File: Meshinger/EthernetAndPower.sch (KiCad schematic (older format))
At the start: 12 parts, among them IC1 FAN53610AUC33X, J1 USB_A, J4 Barrel_Jack_Switch, J5 RJ45_Amphenol_RJMG1BD3B8K1ANR, J6 Conn_02x01, J7 Conn_01x04, U6 1043, U7 1043

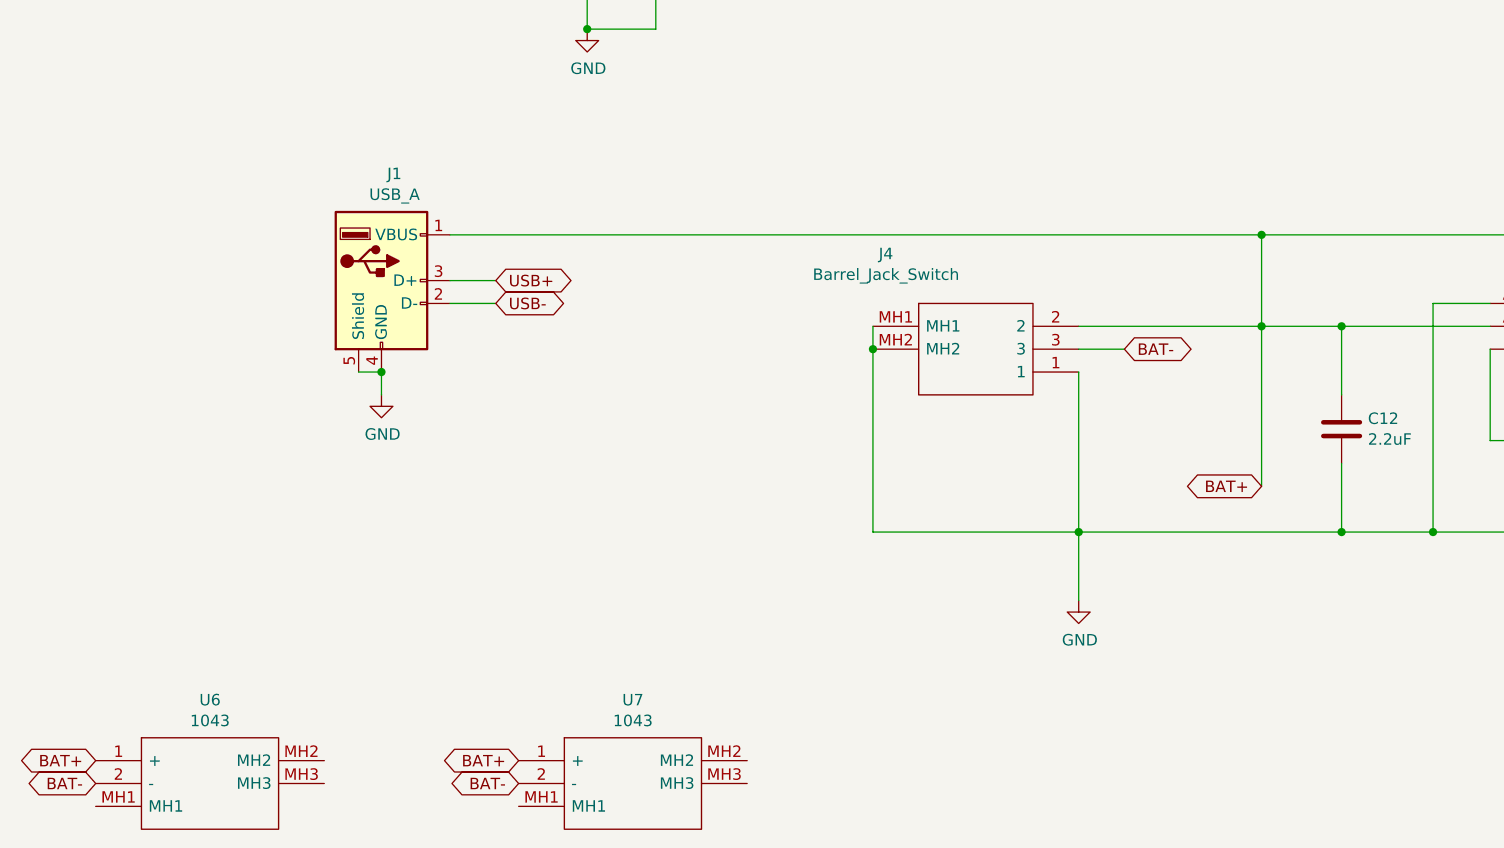
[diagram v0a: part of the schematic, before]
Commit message: Meshinger 1.0 rev C, Display Power MOSFET heats up while off...
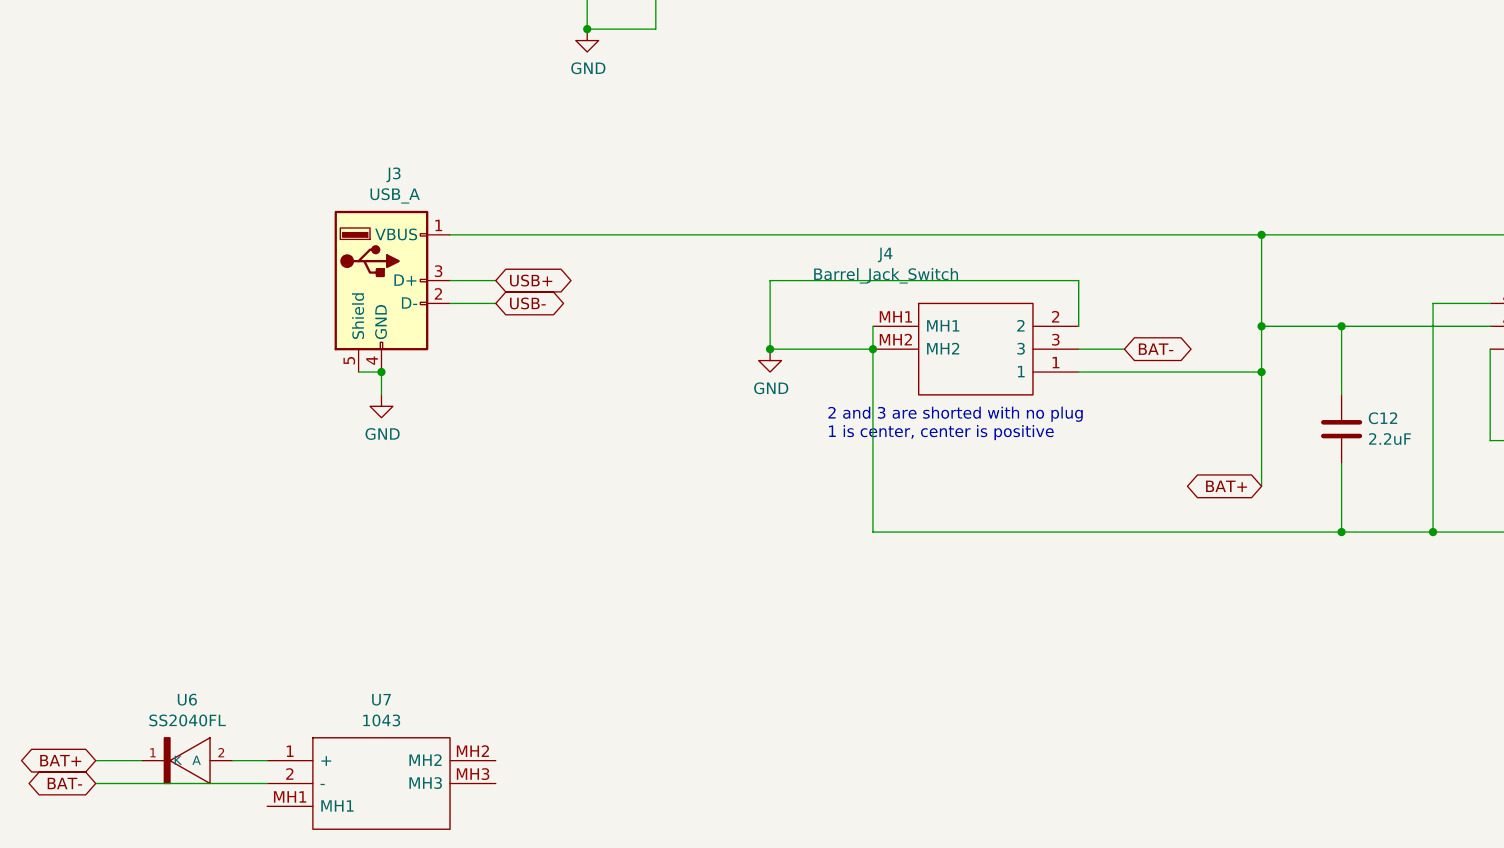
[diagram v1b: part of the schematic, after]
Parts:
- removed U7: 1043, 1043, symbol SamacSys_Parts:1043
- added U6: SS2040FL, SOD-123FL, symbol SS2040FL:SS2040FL
- renumbered J1 to J3, U6 to U7
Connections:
- net BAT+: now also J4.1, U6.1 (K); no longer J4.2, U7.1 (+)
- net GND: now also J4.2; no longer J4.1
- new net: U6.2 (A), U7.1 (+)
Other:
- note added: "2 and 3 are shorted with no plug\n1 is center, center is positive"
- moved on the sheet: U7
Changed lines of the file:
@@
 P 5500 2850
 AR Path="/6040E803/606C8F86" Ref="#PWR?"  Part="1"
-AR Path="/606A5CC1/606C8F86" Ref="#PWR0102"  Part="1"
-F 0 "#PWR0102" H 5500 2600 50  0001 C CNN
+AR Path="/606A5CC1/606C8F86" Ref="#PWR020"  Part="1"
+F 0 "#PWR020" H 5500 2600 50  0001 C CNN
 F 1 "GND" H 5505 2677 50  0000 C CNN
 F 2 "" H 5500 2850 50  0001 C CNN
@@
 P 3300 3250
 AR Path="/6040E803/606C8FA6" Ref="#PWR?"  Part="1"
-AR Path="/606A5CC1/606C8FA6" Ref="#PWR0114"  Part="1"
-F 0 "#PWR0114" H 3300 3000 50  0001 C CNN
+AR Path="/606A5CC1/606C8FA6" Ref="#PWR018"  Part="1"
+F 0 "#PWR018" H 3300 3000 50  0001 C CNN
 F 1 "GND" H 3305 3077 50  0000 C CNN
 F 2 "" H 3300 3250 50  0001 C CNN
@@
 $EndComp
 $Comp
-L Connector:USB_A J1
+L Connector:USB_A J3
 U 1 1 606D792E
 P 2400 4350
-F 0 "J1" H 2457 4817 50  0000 C CNN
+F 0 "J3" H 2457 4817 50  0000 C CNN
 F 1 "USB_A" H 2457 4726 50  0000 C CNN
 F 2 "Connector_USB:USB_A_Stewart_SS-52100-001_Horizontal" H 2550 4300 50  0001 C CNN
@@
 	2300 4750 2400 4750
 $Comp
-L power:GND #PWR0118
+L power:GND #PWR017
 U 1 1 606DDE92
 P 2400 4850
-F 0 "#PWR0118" H 2400 4600 50  0001 C CNN
+F 0 "#PWR017" H 2400 4600 50  0001 C CNN
 F 1 "GND" H 2405 4677 50  0000 C CNN
 F 2 "" H 2400 4850 50  0001 C CNN
@@
 	5450 4650 5650 4650
 $Comp
-L power:GND #PWR0119
+L power:GND #PWR019
 U 1 1 606F6FA3
-P 5450 5750
-F 0 "#PWR0119" H 5450 5500 50  0001 C CNN
-F 1 "GND" H 5455 5577 50  0000 C CNN
-F 2 "" H 5450 5750 50  0001 C CNN
-F 3 "" H 5450 5750 50  0001 C CNN
-	1    5450 5750
-	1    0    0    -1
-$EndComp
-Wire Wire Line
-	6250 5250 6250 4550
-Wire Wire Line
-	5450 4550 6250 4550
+P 4100 4650
+F 0 "#PWR019" H 4100 4400 50  0001 C CNN
+F 1 "GND" H 4105 4477 50  0000 C CNN
+F 2 "" H 4100 4650 50  0001 C CNN
+F 3 "" H 4100 4650 50  0001 C CNN
+	1    4100 4650
+	1    0    0    -1
+$EndComp
+Wire Wire Line
+	6250 5250 6250 4750
 Connection ~ 6250 4550
 Wire Wire Line
 	6250 4550 6250 4150
 Wire Wire Line
-	5450 4750 5450 5450
-Wire Wire Line
 	7250 4450 7000 4450
-Connection ~ 5450 5450
-Wire Wire Line
-	5450 5450 5450 5750
 Wire Wire Line
 	8350 4150 8350 4450
@@
 Wire Wire Line
 	7000 4450 7000 5450
-Wire Wire Line
-	5450 5450 6600 5450
 Connection ~ 7000 5450
 Wire Wire Line
@@
 Connection ~ 9550 5050
 $Comp
-L power:+3.3V #PWR0121
+L power:+3.3V #PWR022
 U 1 1 6073C0C4
 P 10350 5050
-F 0 "#PWR0121" H 10350 4900 50  0001 C CNN
+F 0 "#PWR022" H 10350 4900 50  0001 C CNN
 F 1 "+3.3V" H 10365 5223 50  0000 C CNN
 F 2 "" H 10350 5050 50  0001 C CNN
@@
 	9550 5050 10350 5050
 $Comp
-L power:GND #PWR0122
+L power:GND #PWR021
 U 1 1 607590C0
 P 7250 2050
-F 0 "#PWR0122" H 7250 1800 50  0001 C CNN
+F 0 "#PWR021" H 7250 1800 50  0001 C CNN
 F 1 "GND" H 7255 1877 50  0000 C CNN
 F 2 "" H 7250 2050 50  0001 C CNN
@@
 Wire Wire Line
 	4550 4650 4550 5450
-Wire Wire Line
-	4550 5450 5450 5450
 Connection ~ 4550 4650
 $Comp
@@
 BAT+
 $Comp
-L SamacSys_Parts:1043 U6
+L SamacSys_Parts:1043 U7
 U 1 1 60752788
-P 1150 6450
-F 0 "U6" H 1650 6715 50  0000 C CNN
-F 1 "1043" H 1650 6624 50  0000 C CNN
-F 2 "1043" H 2000 6550 50  0001 L CNN
-F 3 "http://www.keyelco.com/product-pdf.cfm?p=919" H 2000 6450 50  0001 L CNN
-F 4 "KEYSTONE - 1043 - BATTERY HOLDER, 18650, TH" H 2000 6350 50  0001 L CNN "Description"
-F 5 "14.86" H 2000 6250 50  0001 L CNN "Height"
-F 6 "534-1043" H 2000 6150 50  0001 L CNN "Mouser Part Number"
-F 7 "https://www.mouser.co.uk/ProductDetail/Keystone-Electronics/1043?qs=%2F7TOpeL5Mz6j%2FnxeOA1rsg%3D%3D" H 2000 6050 50  0001 L CNN "Mouser Price/Stock"
-F 8 "Keystone Electronics" H 2000 5950 50  0001 L CNN "Manufacturer_Name"
-F 9 "1043" H 2000 5850 50  0001 L CNN "Manufacturer_Part_Number"
-	1    1150 6450
-	1    0    0    -1
-$EndComp
-$Comp
-L SamacSys_Parts:1043 U7
-U 1 1 60753BFA
-P 3000 6450
-F 0 "U7" H 3500 6715 50  0000 C CNN
-F 1 "1043" H 3500 6624 50  0000 C CNN
-F 2 "1043" H 3850 6550 50  0001 L CNN
-F 3 "http://www.keyelco.com/product-pdf.cfm?p=919" H 3850 6450 50  0001 L CNN
-F 4 "KEYSTONE - 1043 - BATTERY HOLDER, 18650, TH" H 3850 6350 50  0001 L CNN "Description"
-F 5 "14.86" H 3850 6250 50  0001 L CNN "Height"
-F 6 "534-1043" H 3850 6150 50  0001 L CNN "Mouser Part Number"
-F 7 "https://www.mouser.co.uk/ProductDetail/Keystone-Electronics/1043?qs=%2F7TOpeL5Mz6j%2FnxeOA1rsg%3D%3D" H 3850 6050 50  0001 L CNN "Mouser Price/Stock"
-F 8 "Keystone Electronics" H 3850 5950 50  0001 L CNN "Manufacturer_Name"
-F 9 "1043" H 3850 5850 50  0001 L CNN "Manufacturer_Part_Number"
-	1    3000 6450
-	1    0    0    -1
-$EndComp
-Text GLabel 3000 6450 0    50   BiDi ~ 0
-BAT+
-Text GLabel 3000 6550 0    50   BiDi ~ 0
-BAT-
+P 1900 6450
+F 0 "U7" H 2400 6715 50  0000 C CNN
+F 1 "1043" H 2400 6624 50  0000 C CNN
+F 2 "1043" H 2750 6550 50  0001 L CNN
+F 3 "http://www.keyelco.com/product-pdf.cfm?p=919" H 2750 6450 50  0001 L CNN
+F 4 "KEYSTONE - 1043 - BATTERY HOLDER, 18650, TH" H 2750 6350 50  0001 L CNN "Description"
+F 5 "14.86" H 2750 6250 50  0001 L CNN "Height"
+F 6 "534-1043" H 2750 6150 50  0001 L CNN "Mouser Part Number"
+F 7 "https://www.mouser.co.uk/ProductDetail/Keystone-Electronics/1043?qs=%2F7TOpeL5Mz6j%2FnxeOA1rsg%3D%3D" H 2750 6050 50  0001 L CNN "Mouser Price/Stock"
+F 8 "Keystone Electronics" H 2750 5950 50  0001 L CNN "Manufacturer_Name"
+F 9 "1043" H 2750 5850 50  0001 L CNN "Manufacturer_Part_Number"
+	1    1900 6450
+	1    0    0    -1
+$EndComp
 Text GLabel 1150 6450 0    50   BiDi ~ 0
 BAT+
@@
 Text GLabel 8150 3050 2    50   BiDi ~ 0
 BAT+
+Text Notes 4350 5050 0    50   ~ 0
+2 and 3 are shorted with no plug\n1 is center, center is positive
+Wire Wire Line
+	4550 5450 6600 5450
+Wire Wire Line
+	5450 4750 6250 4750
+Connection ~ 6250 4750
+Wire Wire Line
+	6250 4750 6250 4550
+Wire Wire Line
+	4100 4650 4100 4350
+Wire Wire Line
+	4100 4350 5450 4350
+Wire Wire Line
+	5450 4350 5450 4550
+Wire Wire Line
+	4550 4650 4100 4650
+Connection ~ 4100 4650
+$Comp
+L SS2040FL:SS2040FL U?
+U 1 1 60FB3A37
+P 1550 6450
+AR Path="/6039D4D4/60FB3A37" Ref="U?"  Part="1"
+AR Path="/606A5CC1/60FB3A37" Ref="U6"  Part="1"
+F 0 "U6" H 1550 6715 50  0000 C CNN
+F 1 "SS2040FL" H 1550 6624 50  0000 C CNN
+F 2 "SOD-123FL" H 1550 6450 50  0001 L BNN
+F 3 "" H 1550 6450 50  0001 L BNN
+	1    1550 6450
+	1    0    0    -1
+$EndComp
+Wire Wire Line
+	1750 6450 1900 6450
+Wire Wire Line
+	1150 6450 1350 6450
+Wire Wire Line
+	1150 6550 1900 6550
 $EndSCHEMATC

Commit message: Meshinger 1.0 rev D, now with power switch and squiggles.
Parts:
- added S1: 1825232-1, 18252321, symbol SamacSys_Parts:1825232-1
- J7: value Conn_01x04 -> Conn_01x03; footprint Connector_PinHeader_2.54mm:PinHeader_1x04_P2.54mm_Vertical -> Connector_PinHeader_2.54mm:PinHeader_1x03_P2.54mm_Vertical; symbol Connector_Generic:Conn_01x04 -> Connector_Generic:Conn_01x03
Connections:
- net GND: now also J7.1 (Pin_1), S1.1, S1.MH1, S1.MH2; no longer J7.2 (Pin_2)
- net HW_RESET: now also S1.2; no longer J7.1 (Pin_1)
- net UART_RX: now also J7.3 (Pin_3); no longer J7.4 (Pin_4)
- net UART_TX: now also J7.2 (Pin_2); no longer J7.3 (Pin_3)
- no-connect marks 2 -> 3
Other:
- moved on the sheet: J6
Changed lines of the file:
@@
 L Connector_Generic:Conn_02x01 J?
 U 1 1 606C8F7A
-P 7850 3050
+P 6900 2700
 AR Path="/6040E803/606C8F7A" Ref="J?"  Part="1"
 AR Path="/606A5CC1/606C8F7A" Ref="J6"  Part="1"
-F 0 "J6" H 7900 3267 50  0000 C CNN
-F 1 "Conn_02x01" H 7900 3176 50  0000 C CNN
-F 2 "Connector_PinHeader_2.54mm:PinHeader_2x01_P2.54mm_Vertical" H 7850 3050 50  0001 C CNN
-F 3 "~" H 7850 3050 50  0001 C CNN
-	1    7850 3050
+F 0 "J6" H 6950 2917 50  0000 C CNN
+F 1 "Conn_02x01" H 6950 2826 50  0000 C CNN
+F 2 "Connector_PinHeader_2.54mm:PinHeader_2x01_P2.54mm_Vertical" H 6900 2700 50  0001 C CNN
+F 3 "~" H 6900 2700 50  0001 C CNN
+	1    6900 2700
 	1    0    0    -1
 $EndComp
@@
 L power:GND #PWR021
 U 1 1 607590C0
-P 7250 2050
-F 0 "#PWR021" H 7250 1800 50  0001 C CNN
-F 1 "GND" H 7255 1877 50  0000 C CNN
-F 2 "" H 7250 2050 50  0001 C CNN
-F 3 "" H 7250 2050 50  0001 C CNN
-	1    7250 2050
-	1    0    0    -1
-$EndComp
-Text GLabel 7850 2250 0    50   BiDi ~ 0
+P 6300 1700
+F 0 "#PWR021" H 6300 1450 50  0001 C CNN
+F 1 "GND" H 6305 1527 50  0000 C CNN
+F 2 "" H 6300 1700 50  0001 C CNN
+F 3 "" H 6300 1700 50  0001 C CNN
+	1    6300 1700
+	1    0    0    -1
+$EndComp
+Text GLabel 6900 1900 0    50   BiDi ~ 0
 UART_RX
-Text GLabel 7850 2150 0    50   BiDi ~ 0
+Text GLabel 6900 1800 0    50   BiDi ~ 0
 UART_TX
-Text GLabel 7850 1950 0    50   BiDi ~ 0
-HW_RESET
-Wire Wire Line
-	7250 2050 7850 2050
+Wire Wire Line
+	6300 1700 6900 1700
 Wire Wire Line
 	4550 4550 4550 4650
@@
 Connection ~ 4550 4650
 $Comp
-L Connector_Generic:Conn_01x04 J7
+L Connector_Generic:Conn_01x03 J7
 U 1 1 607590C9
-P 8050 2050
-F 0 "J7" H 8130 2042 50  0000 L CNN
-F 1 "Conn_01x04" H 8130 1951 50  0000 L CNN
-F 2 "Connector_PinHeader_2.54mm:PinHeader_1x04_P2.54mm_Vertical" H 8050 2050 50  0001 C CNN
-F 3 "~" H 8050 2050 50  0001 C CNN
-	1    8050 2050
+P 7100 1800
+F 0 "J7" H 7180 1792 50  0000 L CNN
+F 1 "Conn_01x03" H 7180 1701 50  0000 L CNN
+F 2 "Connector_PinHeader_2.54mm:PinHeader_1x03_P2.54mm_Vertical" H 7100 1800 50  0001 C CNN
+F 3 "~" H 7100 1800 50  0001 C CNN
+	1    7100 1800
 	1    0    0    -1
 $EndComp
@@
 Text GLabel 1150 6550 0    50   BiDi ~ 0
 BAT-
-Text GLabel 7650 3050 0    50   BiDi ~ 0
+Text GLabel 6700 2700 0    50   BiDi ~ 0
 BAT-
-Text GLabel 8150 3050 2    50   BiDi ~ 0
+Text GLabel 7200 2700 2    50   BiDi ~ 0
 BAT+
 Text Notes 4350 5050 0    50   ~ 0
@@
 Wire Wire Line
 	1150 6550 1900 6550
+Text GLabel 8350 2300 0    50   BiDi ~ 0
+HW_RESET
+$Comp
+L power:GND #PWR0101
+U 1 1 621657AE
+P 8500 2650
+F 0 "#PWR0101" H 8500 2400 50  0001 C CNN
+F 1 "GND" H 8505 2477 50  0000 C CNN
+F 2 "" H 8500 2650 50  0001 C CNN
+F 3 "" H 8500 2650 50  0001 C CNN
+	1    8500 2650
+	1    0    0    -1
+$EndComp
+$Comp
+L SamacSys_Parts:1825232-1 S1
+U 1 1 6215EB45
+P 8750 2100
+F 0 "S1" H 9478 1946 50  0000 L CNN
+F 1 "1825232-1" H 9478 1855 50  0000 L CNN
+F 2 "18252321" H 9500 2200 50  0001 L CNN
+F 3 "https://componentsearchengine.com/Datasheets/1/1825232-1.pdf" H 9500 2100 50  0001 L CNN
+F 4 "TE CONNECTIVITY - 1825232-1 - SLIDE SWITCH, SPDT, 0.2A, 30VDC, SOLDER" H 9500 2000 50  0001 L CNN "Description"
+F 5 "3.7" H 9500 1900 50  0001 L CNN "Height"
+F 6 "655-1825232-1" H 9500 1800 50  0001 L CNN "Mouser Part Number"
+F 7 "https://www.mouser.co.uk/ProductDetail/TE-Connectivity-PB/1825232-1?qs=kTKVN3NWb5FosGxaNC1%252BtA%3D%3D" H 9500 1700 50  0001 L CNN "Mouser Price/Stock"
+F 8 "TE Connectivity" H 9500 1600 50  0001 L CNN "Manufacturer_Name"
+F 9 "1825232-1" H 9500 1500 50  0001 L CNN "Manufacturer_Part_Number"
+	1    8750 2100
+	1    0    0    -1
+$EndComp
+Wire Wire Line
+	8750 2100 8500 2100
+Wire Wire Line
+	8750 2500 8500 2500
+Connection ~ 8500 2500
+Wire Wire Line
+	8500 2500 8500 2650
+NoConn ~ 8750 2400
+Wire Wire Line
+	8500 2100 8500 2200
+Wire Wire Line
+	8350 2300 8750 2300
+Wire Wire Line
+	8750 2200 8500 2200
+Connection ~ 8500 2200
+Wire Wire Line
+	8500 2200 8500 2500
 $EndSCHEMATC
